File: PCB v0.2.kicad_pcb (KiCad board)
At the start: 2 copper layers, 77.4 x 97 mm, 60 parts, among them J1 XT60-M, J10 Screw 2.54mm 5P, J11 Screw 2.54mm 5P, J12 Screw 2.54mm 5P, J13 2.54mm 3P, J14 2.54mm 3P, J15 2.54mm 3P, J16 2.54mm 3P, J17 JST-SH 3P, J18 JST-SH 3P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

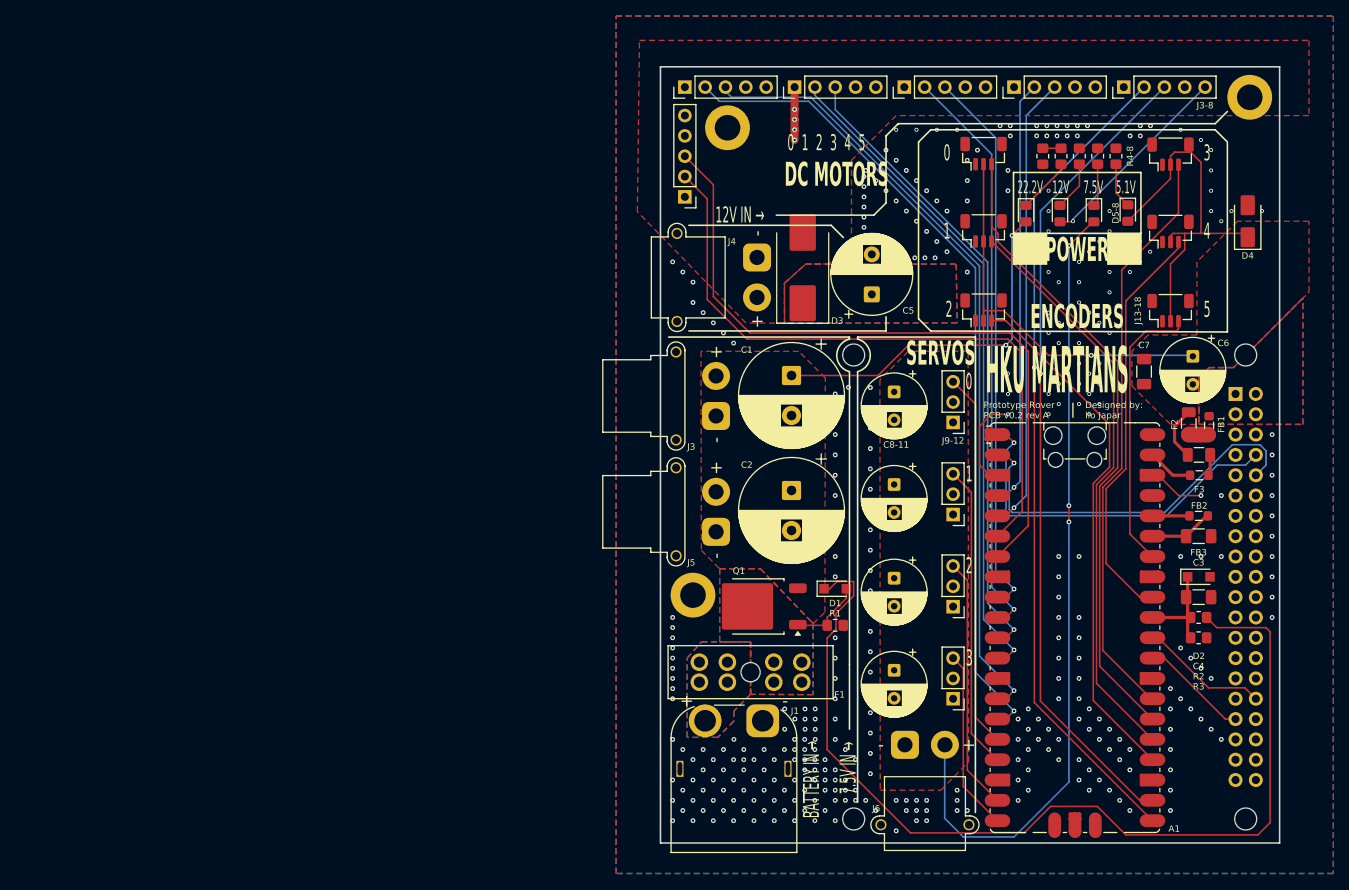
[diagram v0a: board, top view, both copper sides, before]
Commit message: U1 symbol was not in v0.2
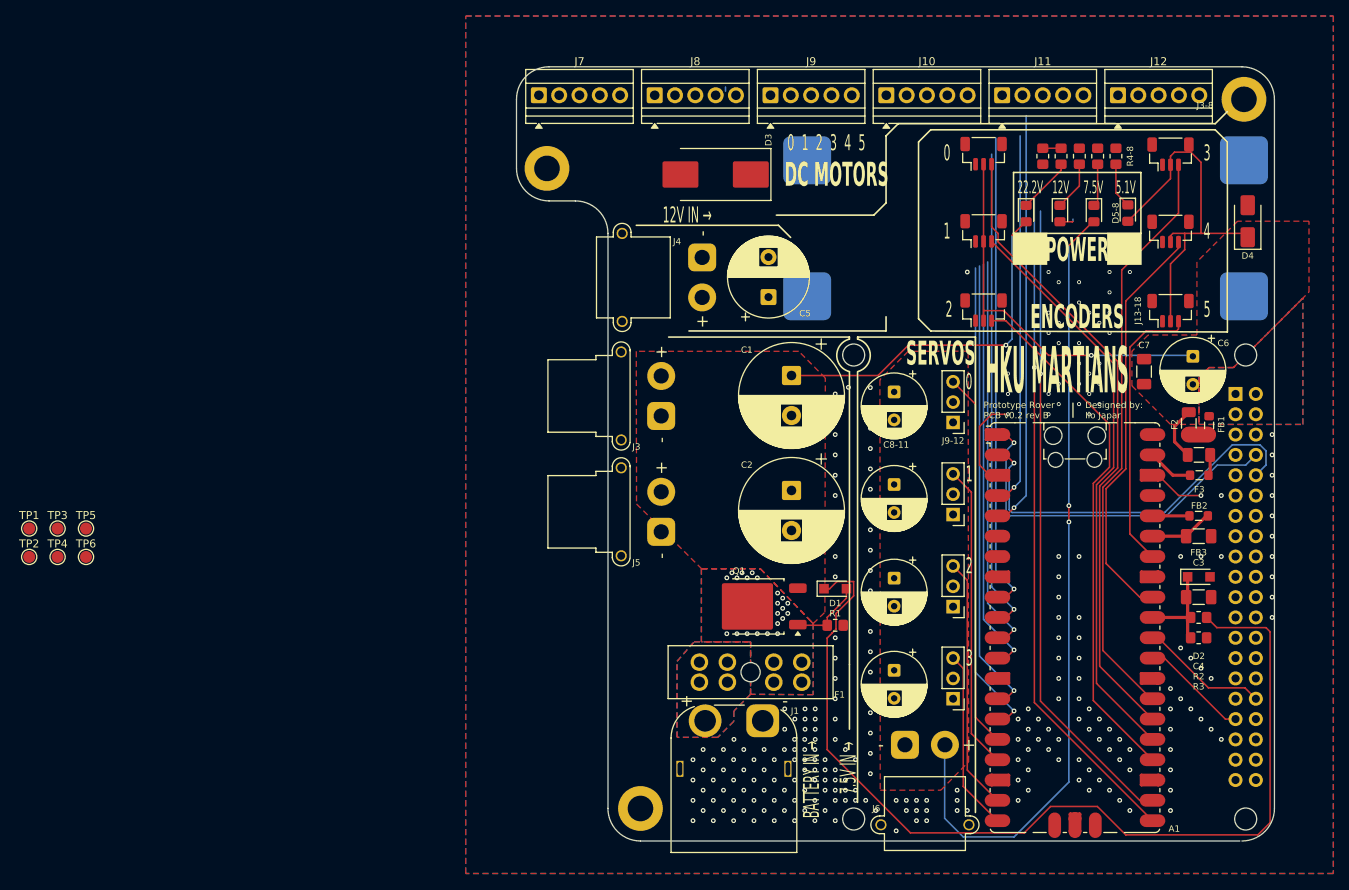
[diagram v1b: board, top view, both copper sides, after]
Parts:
- added TP1: TestPoint, TestPoint:TestPoint_Pad_D1.5mm, F.Cu at (31.5, 102.4)
- added TP2: TestPoint, TestPoint:TestPoint_Pad_D1.5mm, F.Cu at (31.5, 106.0)
- added TP3: TestPoint, TestPoint:TestPoint_Pad_D1.5mm, F.Cu at (35.1, 102.4)
- added TP4: TestPoint, TestPoint:TestPoint_Pad_D1.5mm, F.Cu at (35.1, 106.0)
- added TP5: TestPoint, TestPoint:TestPoint_Pad_D1.5mm, F.Cu at (38.6, 102.4)
- added TP6: TestPoint, TestPoint:TestPoint_Pad_D1.5mm, F.Cu at (38.6, 106.0)
- added U1: 3.2~32V -> 5.1V 5A, Library:Buck_Converter_54x24mm, B.Cu at (156.0, 67.8)
- J10, J11, J12, J7, J8, J9: footprint Connector_PinHeader_2.54mm:PinHeader_1x05_P2.54mm_Vertical -> TerminalBlock:TerminalBlock_Xinya_XY308-2.54-5P_1x05_P2.54mm_Horizontal
- moved H2 27.5 mm to (108.0, 137.4)
- moved H1 23.1 mm to (96.3, 57.4)
- moved J7 22.2 mm to (95.2, 48.3), turned to 0 degrees
- moved D3 16.0 mm to (117.3, 58.2), turned to 180 degrees
- moved C5 12.9 mm to (124.0, 73.5)
- moved J3 6.86 mm to (110.5, 88.4)
- moved J4 6.86 mm to (115.7, 68.5)
- moved J5 6.86 mm to (110.5, 102.8)
- moved J8 3.91 mm to (109.7, 48.3), turned to 0 degrees
- moved J9 3.18 mm to (124.2, 48.3), turned to 0 degrees
- moved J10 2.47 mm to (138.7, 48.3), turned to 0 degrees
- moved J11 1.80 mm to (153.2, 48.3), turned to 0 degrees
- moved J12 1.25 mm to (167.6, 48.3), turned to 0 degrees
- moved H3 0.77 mm to (183.4, 48.8)
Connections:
- J17 pad MP: GND -> (no net)
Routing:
- net /BLDC_0: track 89.5 -> 0.00 mm
- net /REV_0: track 83.9 -> 0.00 mm
- net /REV_1: track 102.0 -> 58.8 mm
- net /BLDC_1: track 97.6 -> 56.8 mm
- net /REV_2: track 83.2 -> 52.3 mm
- net /BLDC_2: track 79.6 -> 49.8 mm
- net +12V: track 25.3 -> 1.91 mm, vias 1 -> 0
- net /BLDC_5: track 102.3 -> 80.4 mm
- net /REV_5: track 103.5 -> 84.1 mm
- net /REV_3: track 72.4 -> 60.5 mm
- net /BLDC_3: track 68.8 -> 59.8 mm
- net /REV_4: track 53.6 -> 46.7 mm
- net GND: track 25.5 -> 18.9 mm, vias 361 -> 252
- net /BLDC_4: track 57.2 -> 52.1 mm
- net Net-(Q1-D): vias 0 -> 22
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- removed copper zone on F.Cu, net +12V
- removed copper zone on B.Cu, net Net-(D3-K)
- removed copper zone on F.Cu, net Net-(D3-K)
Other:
- board size 77.4 x 97 mm -> 94.7 x 96.8 mm
- board text added: "Prototype Rover PCB v0.2 rev B"
- board text removed: "Prototype Rover PCB v0.2 rev A"
